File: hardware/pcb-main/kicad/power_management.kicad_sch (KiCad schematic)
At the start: 51 parts, among them J7 TYPE-C-31-M-12, J8 JST_PH_2pin, Q2 PMOS, U5 BQ24195RGER, U6 TPS61088RHLR, U7 INA219AIDCNR

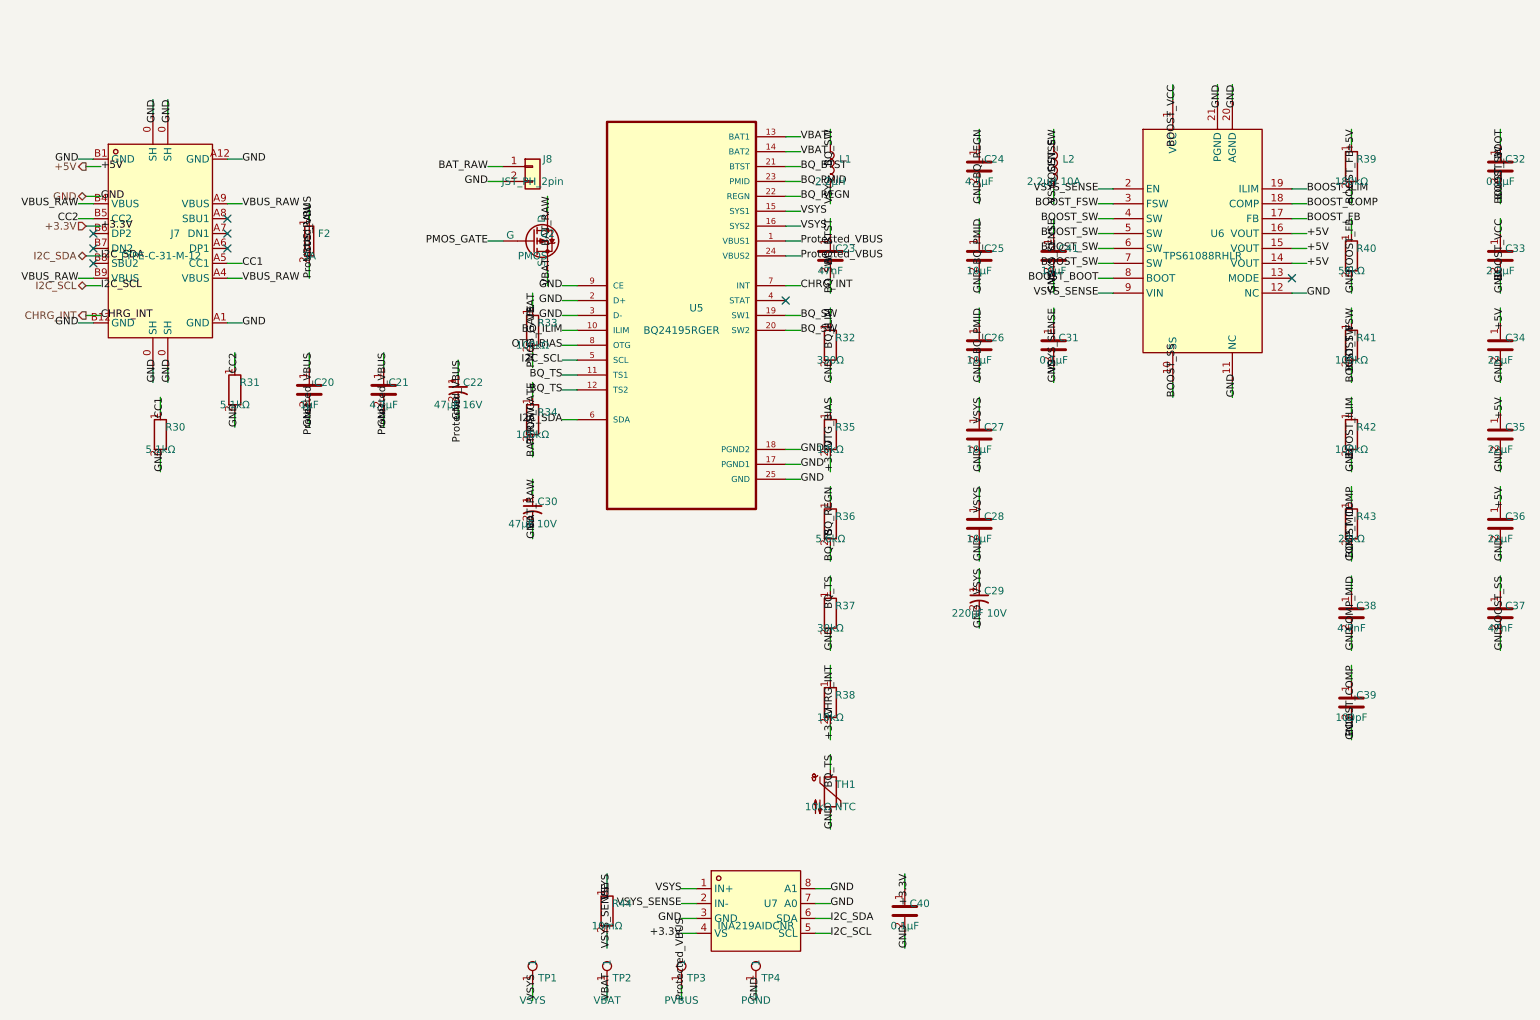
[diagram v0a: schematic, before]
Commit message: Integrate power management sub-sheet into root schematic (Phase 3.6)
- Delete J2 (DWEII USB-C module) and D1 (Schottky) from root sheet
- Add hierarchical sheet reference to power_management.kicad_sch
- Wire 6 sheet pins: +5V, GND, +3.3V, I2C_SDA, I2C_SCL, CHRG_INT
- Connect CHRG_INT to GPIO 21 (U2 pin 19)
- Hide non-essential property labels (Description, Datasheet, etc.)
  across all original schematic sheets — only Reference and Value visible
- ERC: 0 errors on root/LED/TCA9548A sheets, 4 expected power_pin
  warnings on power management sheet (net labels vs PWR_FLAG)

Made-with: Cursor
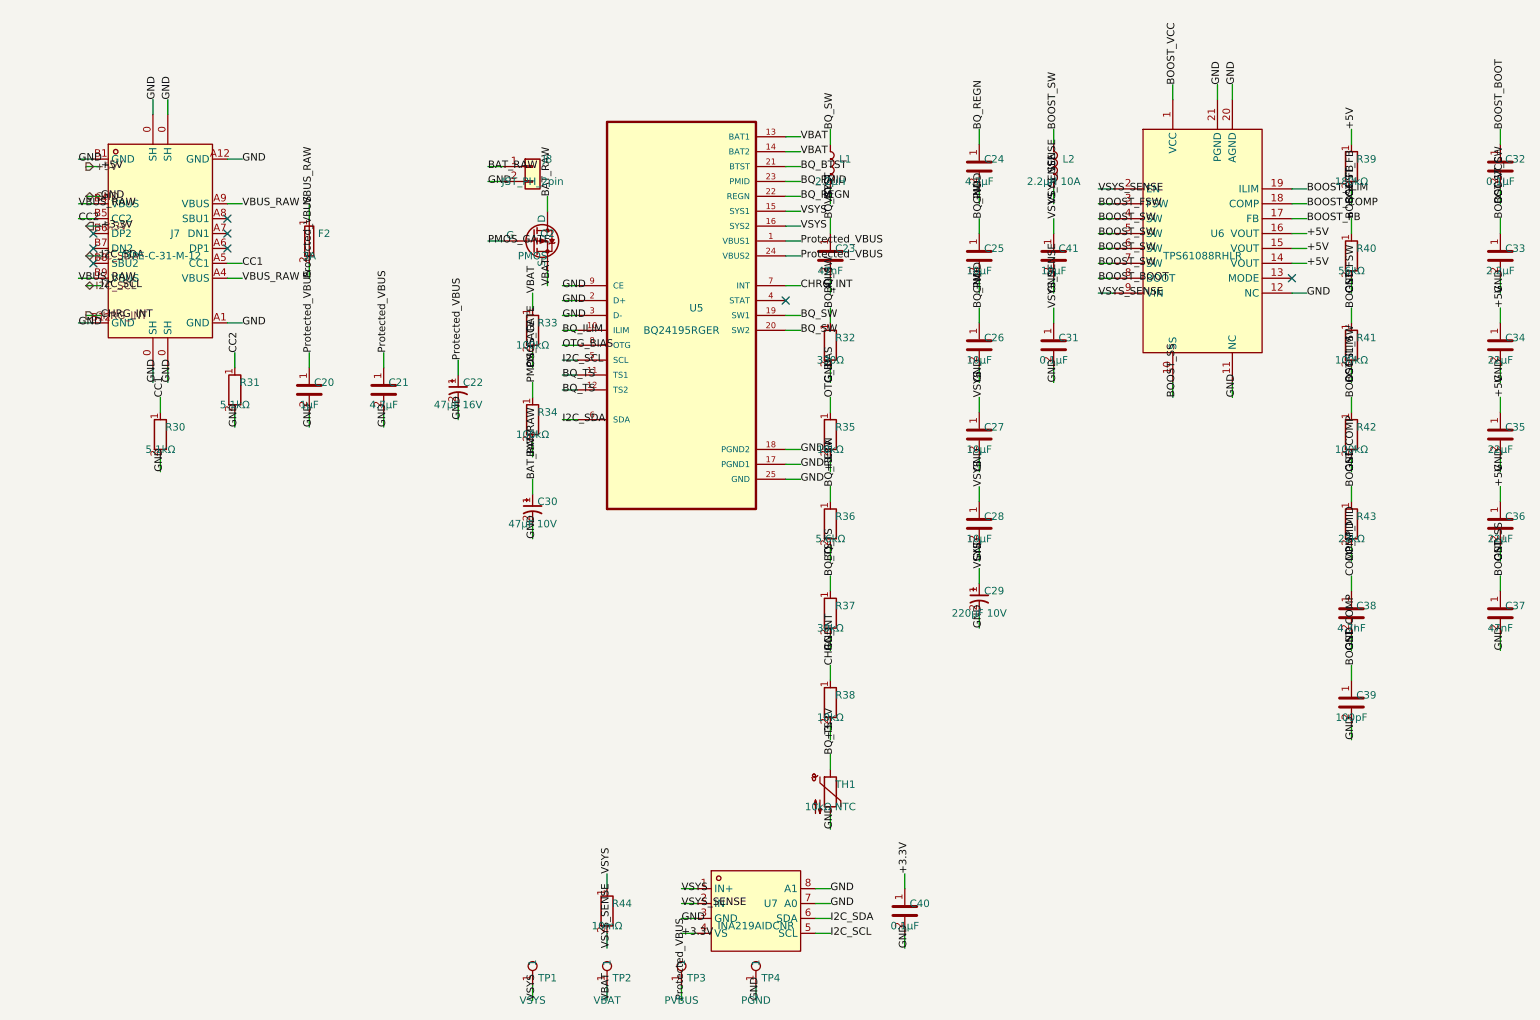
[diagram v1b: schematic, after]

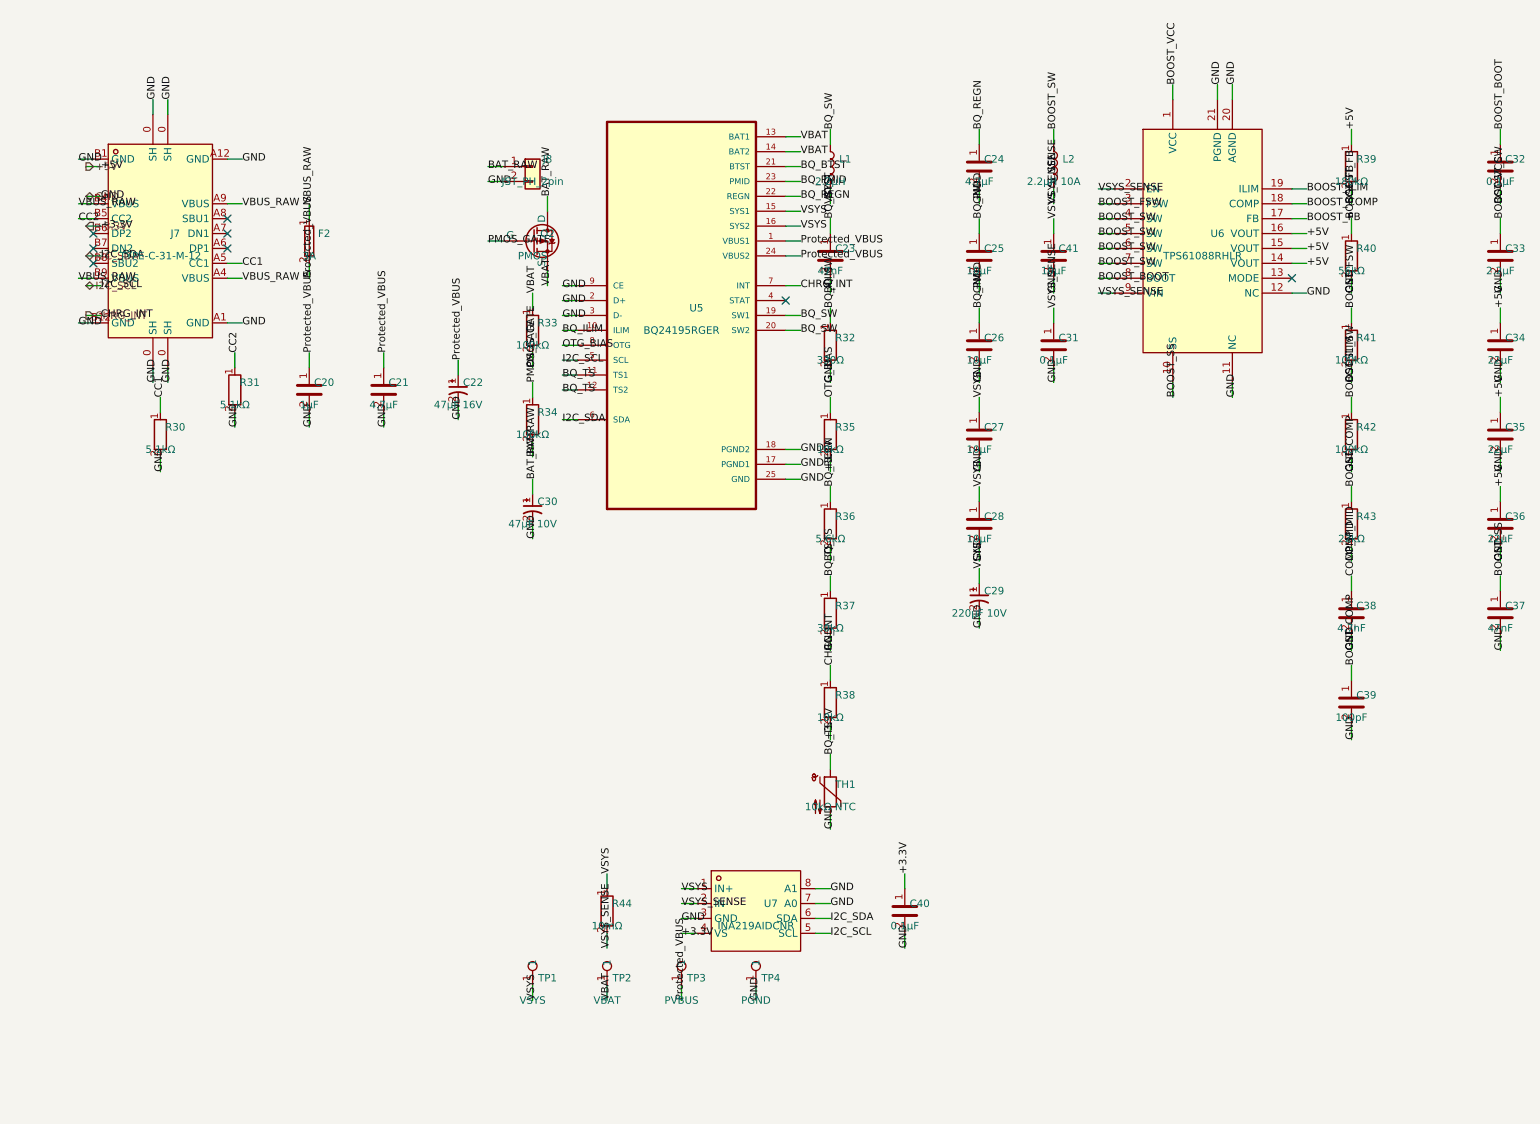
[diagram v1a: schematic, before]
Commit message: Fix ERC power_pin_not_driven errors with PWR_FLAG symbols (Phase 3.7)
Add 4 PWR_FLAG symbols (#FLG05-08) to resolve power_pin_not_driven ERC
errors on VBUS_RAW, Protected_VBUS, VBAT, and VSYS nets. Fix instance
path format to use /{root_uuid}/{sheet_ref_uuid} matching KiCad 9's
hierarchical sheet convention. ERC now reports 0 errors, 31 warnings
(all cosmetic pin_to_pin type mismatches from easyeda2kicad symbols).

Also checks off Phase 3 tasks 3.3-3.7 in TASKS.md with completion notes.

Made-with: Cursor
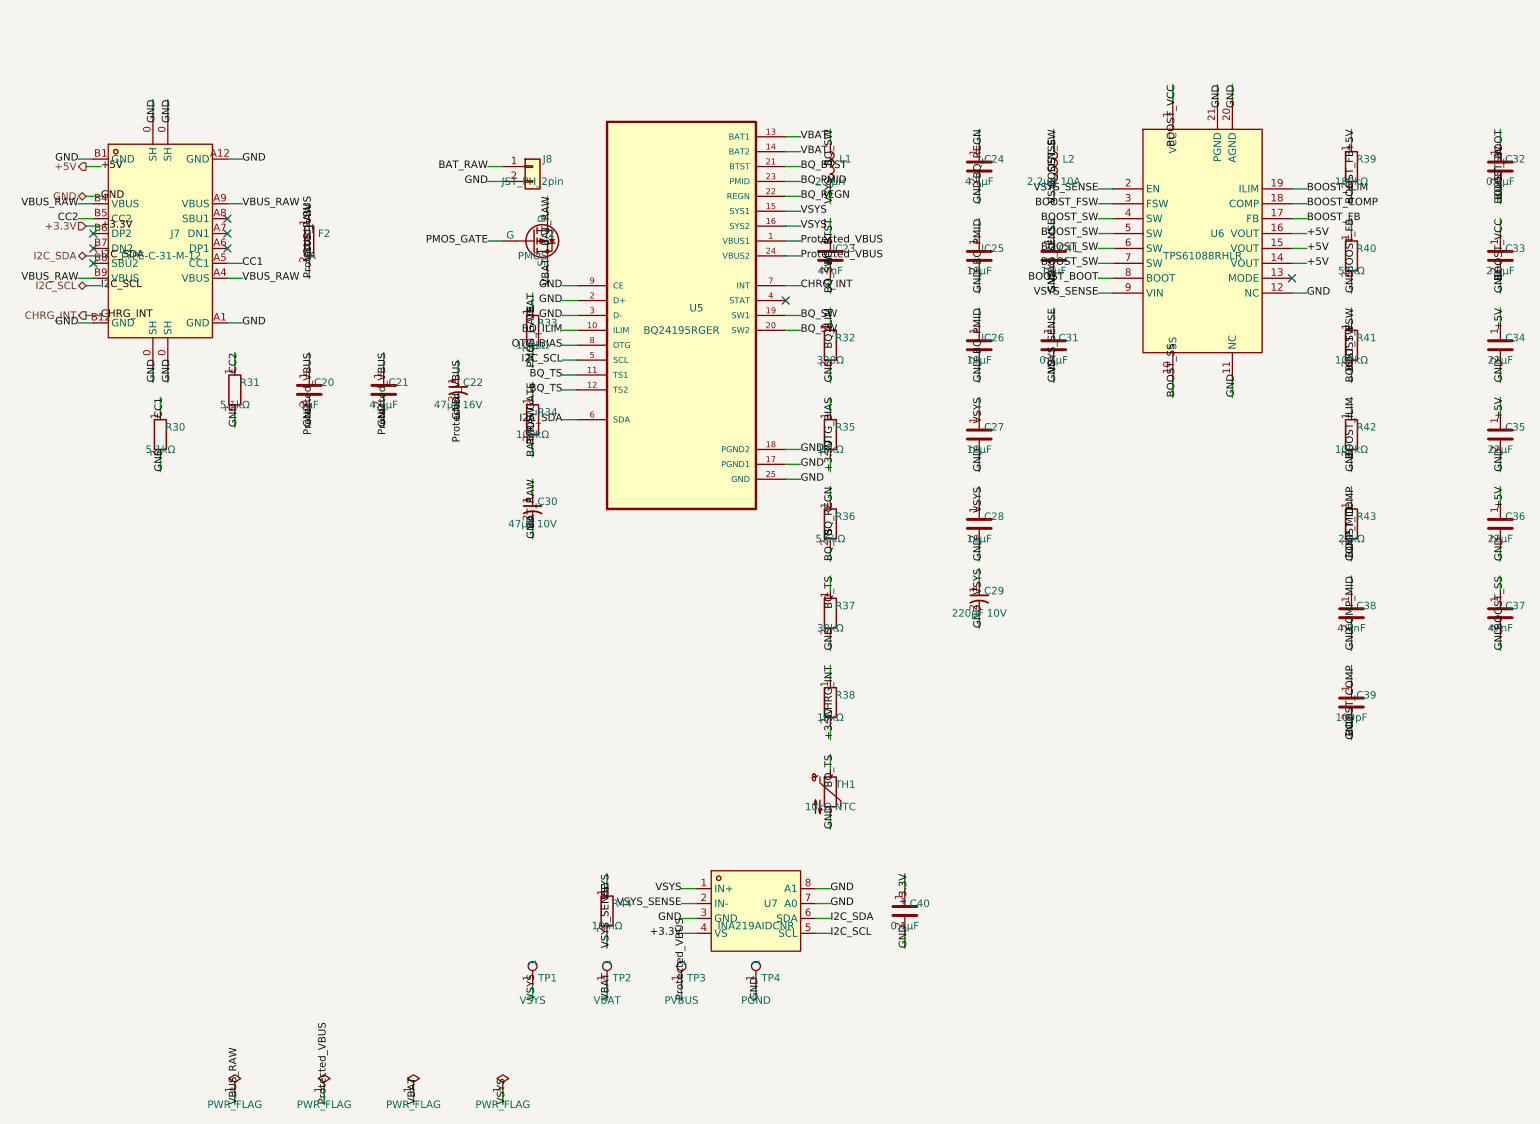
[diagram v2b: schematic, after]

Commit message: Add AI annotations and context review for power management components (Phase 4)
Phase 4 of integrated power initiative: extracted circuit-context.json with
all 55 new power management components, performed pin-by-pin review against
spec with zero discrepancies, and wrote AI annotations for all 51 physical
components plus updated TPIO21 (GPIO 21 now CHRG_INT). 86/86 components
annotated (100% coverage). Added 6 block definitions, annotated 26 nets,
and updated stale descriptions from pre-power-management era.

Made-with: Cursor
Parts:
- C20: ai_block (none) -> usb_c_input; ai_critical_specs (none) -> 1uF X7R, place within 3mm of U5; ai_function (none) -> High-frequency bypass on Protected_VBUS, close to U5 VBUS p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; ai_role (none) -> decoupling
- C21: ai_block (none) -> usb_c_input; ai_critical_specs (none) -> 4.7uF X5R; ai_function (none) -> Ceramic decoupling on Protected_VBUS rail; ai_role (none) -> decoupling
- C22: ai_block (none) -> usb_c_input; ai_critical_specs (none) -> 47uF 16V electrolytic; ai_function (none) -> Bulk decoupling on Protected_VBUS rail; ai_role (none) -> decoupling
- C23: ai_block (none) -> battery_mgmt; ai_critical_specs (none) -> 47nF per datasheet; ai_function (none) -> BQ24195 bootstrap capacitor (BTST to SW); ai_role (none) -> bootstrap
- C24: ai_block (none) -> battery_mgmt; ai_critical_specs (none) -> 4.7uF; ai_function (none) -> BQ24195 REGN internal LDO bypass; ai_role (none) -> decoupling
- C25, C26: ai_block (none) -> battery_mgmt; ai_critical_specs (none) -> 10uF, C25+C26=20uF meets datasheet minimum; ai_function (none) -> BQ24195 PMID bypass capacitor; ai_role (none) -> decoupling
- C27, C28: ai_block (none) -> battery_mgmt; ai_critical_specs (none) -> 10uF; ai_function (none) -> VSYS rail ceramic decoupling; ai_role (none) -> decoupling
- C29: ai_block (none) -> battery_mgmt; ai_critical_specs (none) -> 220uF 10V electrolytic; ai_function (none) -> VSYS rail bulk output capacitor; ai_role (none) -> decoupling
- C30: ai_block (none) -> battery_mgmt; ai_critical_specs (none) -> 47uF 10V electrolytic; ai_function (none) -> Battery terminal bulk capacitor; ai_role (none) -> decoupling
- C31: ai_block (none) -> boost_5v; ai_critical_specs (none) -> 0.1uF X7R, place within 3mm of U6; ai_function (none) -> VIN pin bypass capacitor, close to U6 pin 9; ai_role (none) -> decoupling
- C32: ai_block (none) -> boost_5v; ai_critical_specs (none) -> 0.1uF; ai_function (none) -> Bootstrap capacitor (BOOT to SW); ai_role (none) -> bootstrap
- C33: ai_block (none) -> boost_5v; ai_critical_specs (none) -> 2.2uF; ai_function (none) -> VCC internal LDO decoupling; ai_role (none) -> decoupling
- C34, C35, C36: ai_block (none) -> boost_5v; ai_critical_specs (none) -> 22uF 0805, 3x parallel = 66uF total; ai_function (none) -> Boost output capacitor; ai_role (none) -> decoupling
- C37: ai_block (none) -> boost_5v; ai_critical_specs (none) -> 47nF; ai_function (none) -> Soft-start timing capacitor (~11ms ramp); ai_role (none) -> timing
- C38: ai_block (none) -> boost_5v; ai_critical_specs (none) -> 4.7nF, bench-tunable 2.2-10nF; ai_function (none) -> Compensation capacitor C_COMP1 (series with R43); ai_role (none) -> compensation
- C39: ai_block (none) -> boost_5v; ai_critical_specs (none) -> 100pF C0G, remove if causing issues; ai_function (none) -> Compensation capacitor C_COMP2 (HF pole); ai_role (none) -> compensation
- C40: ai_block (none) -> power_monitor; ai_critical_specs (none) -> 0.1uF, place within 3mm of U7; ai_function (none) -> INA219 VS supply bypass, close to U7 pin 4; ai_role (none) -> decoupling
- C41: ai_block (none) -> boost_5v; ai_critical_specs (none) -> 10uF 0805; ai_function (none) -> VIN power stage bulk input capacitor; ai_role (none) -> decoupling
- F2: ai_block (none) -> usb_c_input; ai_critical_specs (none) -> 3A rated, 1206 package; ai_function (none) -> VBUS overcurrent protection fuse; ai_role (none) -> protection
- J7: ai_block (none) -> usb_c_input; ai_critical_specs (none) -> TYPE-C-31-M-12, 5.1k CC pull-downs for UFP sink role; ai_function (none) -> USB-C power input connector, 5V sink-only (no data); ai_role (none) -> connector
- J8: ai_block (none) -> battery_mgmt; ai_critical_specs (none) -> JST PH 2-pin, reverse polarity protected by Q2; ai_function (none) -> Battery connector for single-cell Li-ion (Samsung 30Q); ai_role (none) -> connector
- L1: ai_block (none) -> battery_mgmt; ai_critical_specs (none) -> 2.2uH, FNR6028S; ai_function (none) -> BQ24195 buck switching inductor; ai_role (none) -> inductor
- L2: ai_block (none) -> boost_5v; ai_critical_specs (none) -> 2.2uH 10A Isat, FXL0630-2R2-M, minimize trace to U6 SW/VIN; ai_function (none) -> Boost converter power inductor; ai_role (none) -> inductor
- Q2: ai_block (none) -> battery_mgmt; ai_critical_specs (none) -> PMOS SOT-23, D=BAT_RAW S=VBAT, biased by R33/R34 divider; ai_function (none) -> Battery reverse polarity protection MOSFET; ai_role (none) -> protection
- R30: ai_block (none) -> usb_c_input; ai_critical_specs (none) -> 5.1k, required by USB-C spec for sink role; ai_function (none) -> USB-C CC1 pull-down for UFP sink detection; ai_role (none) -> pull_down
- R31: ai_block (none) -> usb_c_input; ai_critical_specs (none) -> 5.1k, required by USB-C spec for sink role; ai_function (none) -> USB-C CC2 pull-down for UFP sink detection; ai_role (none) -> pull_down
- R32: ai_block (none) -> battery_mgmt; ai_critical_specs (none) -> 330R (not 2.7k from reference), ~1.5A ceiling; ai_function (none) -> BQ24195 ILIM resistor, sets hardware input current ceiling; ai_role (none) -> current_limit
- R33: ai_block (none) -> battery_mgmt; ai_critical_specs (none) -> 100k; ai_function (none) -> PMOS gate bias resistor to VBAT (keeps Q2 on when battery p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; ai_role (none) -> bias
- R34: ai_block (none) -> battery_mgmt; ai_critical_specs (none) -> 100k; ai_function (none) -> PMOS gate bias resistor to BAT_RAW (turns Q2 off if reverse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; ai_role (none) -> bias
- R35: ai_block (none) -> battery_mgmt; ai_critical_specs (none) -> 10k to +3.3V, critical for USB-only boot; ai_function (none) -> OTG pin pull-up to +3.3V, sets 500mA SDP boot-time current; ai_role (none) -> pull_up
- R36: ai_block (none) -> battery_mgmt; ai_critical_specs (none) -> 5.6k from BQ_REGN; ai_function (none) -> NTC bias top resistor (REGN to TS), part of temperature mon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; ai_role (none) -> bias
- R37: ai_block (none) -> battery_mgmt; ai_critical_specs (none) -> 30k, replace with 10k if TH1 not populated; ai_function (none) -> NTC bias bottom resistor (TS to GND), parallel with TH1; ai_role (none) -> bias
- R38: ai_block (none) -> battery_mgmt; ai_critical_specs (none) -> 10k to +3.3V, active-low open-drain output; ai_function (none) -> BQ24195 INT pull-up to +3.3V; ai_role (none) -> pull_up
- R39: ai_block (none) -> boost_5v; ai_critical_specs (none) -> 180k 1%, VOUT=1.204*(1+180/56); ai_function (none) -> Feedback divider top resistor (sets 5.07V output); ai_role (none) -> voltage_divider
- R40: ai_block (none) -> boost_5v; ai_critical_specs (none) -> 56k 1%; ai_function (none) -> Feedback divider bottom resistor; ai_role (none) -> voltage_divider
- R41: ai_block (none) -> boost_5v; ai_critical_specs (none) -> 100k, ~2.2MHz; ai_function (none) -> Switching frequency set resistor (FSW to SW); ai_role (none) -> frequency_set
- R42: ai_block (none) -> boost_5v; ai_critical_specs (none) -> 100k, ~11.9A peak; ai_function (none) -> Peak current limit set resistor (ILIM to GND); ai_role (none) -> current_limit
- R43: ai_block (none) -> boost_5v; ai_critical_specs (none) -> 22k, bench-tunable 10-47k; ai_function (none) -> Compensation network resistor; ai_role (none) -> compensation
- R44: ai_block (none) -> power_monitor; ai_critical_specs (none) -> 10mR 1% 1W 2512, Kelvin connection recommended; ai_function (none) -> VSYS current sense shunt resistor between VSYS and VSYS_SEN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; ai_role (none) -> current_sense
- TH1: ai_block (none) -> battery_mgmt; ai_critical_specs (none) -> 10k NTC, biased by R36/R37 divider from REGN; ai_function (none) -> Battery temperature monitoring NTC for BQ24195 TS input; ai_role (none) -> sensor
- TP1: ai_block (none) -> power_test_points; ai_function (none) -> VSYS rail test point (BQ24195 system output, 3.0-4.5V); ai_role (none) -> test_point
- TP2: ai_block (none) -> power_test_points; ai_function (none) -> VBAT rail test point (battery voltage after PMOS); ai_role (none) -> test_point
- TP3: ai_block (none) -> power_test_points; ai_function (none) -> Protected_VBUS test point (USB VBUS after fuse); ai_role (none) -> test_point
- TP4: ai_block (none) -> power_test_points; ai_function (none) -> Power ground test point; ai_role (none) -> test_point
- U5: ai_block (none) -> battery_mgmt; ai_critical_specs (none) -> BQ24195RGER, I2C 0x6B, 4.2V charge, ILIM 330R for ~1.5A cei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; ai_function (none) -> Battery charger and power path manager, provides VSYS from 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; ai_role (none) -> charger_pmic
- U6: ai_block (none) -> boost_5v; ai_critical_specs (none) -> TPS61088RHLR, 10A switch, 5.07V output, 2.2MHz, PFM mode; ai_function (none) -> Synchronous boost converter, VSYS to +5V for entire system; ai_role (none) -> voltage_regulator
- U7: ai_block (none) -> power_monitor; ai_critical_specs (none) -> INA219AIDCNR, I2C 0x40, PGA /2 (+/-80mV), 1mA/LSB, 8A max; ai_function (none) -> I2C power monitor on VSYS rail, measures voltage and current; ai_role (none) -> power_monitor
